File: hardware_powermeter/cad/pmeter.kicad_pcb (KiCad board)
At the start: 4 copper layers, 60 x 16 mm, 57 parts, among them J101 conector magnetico 6 vias, J102 JST SM02B-SRSS-TB, J201 Tag-Connect TC2030-NL, J301 furos da ponte, U101 nPM1100-QDAB, U102 MAX17048G+T10, U201 MinewSemi ME54BS13, U301 ADS1220IRVAR, U302 TPS22916BYFPR, U401 BMA400, U402 TMP117AIDRVR

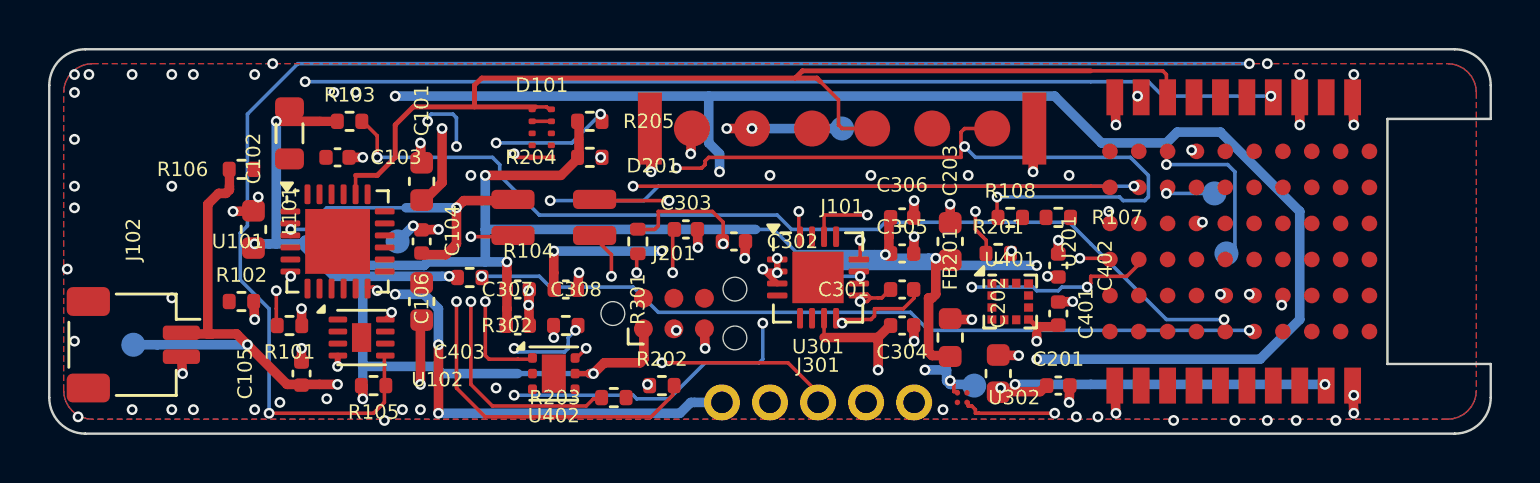
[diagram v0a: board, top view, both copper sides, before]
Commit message: feat(hardware): 48 x 16 mm board and a 53,4 x 19,4 x 8,5 mm pod
The board came down from 60 to 48 mm and the pod from 65,4 x 19,4 x 10,5
to 53,4 x 19,4 x 8,5, with the mass estimate at 11,4 g against the 20 g
of the class. The height now meets the target exactly, because the cell
shrank from 4,0 to 2,5 mm: the owner's 5 kOhm decision takes the meter
from 3,9 to 1,5 mA while pedalling, so 50 hours ask for about 75 mAh and
a 100 mAh pouch is enough. The six-way connector stays, in two rows of
three instead of a single row, which gave back about 7 mm of length
without losing a way, and the Tag-Connect went: with SWD on the cable it
was duplicated copper.

It is NOT manufacturable yet, and the numbers say why rather than a
hopeful adjective: the design rule check finds 0 errors but 16
connections still open. One of them, ERR_N, has no copper at all while
the router reported "98 routed, 0 nets left out", so the router's own
accounting is wrong, not just its routing. Disabling the pruning of
dangling tracks was tried first and changed nothing, which clears the
pruning. A second routing pass made it worse, 21 open and three pairs of
vias too close: the pass is not incremental, it re-routes from scratch
into a different result.

Two more real defects are recorded: the placer cannot seat C403 and
C308, carrying them 11 to 13 mm from the part they decouple, and three
pod rules fail, the back-face bodies against the cell, the rib at zero
and a back pad under a pillar.

The layer drawings print properly for the first time. kicad-cli 8.0.6
does not have --page-size-mode or --exclude-drawing-sheet, which are
KiCad 9 options, so the export was failing outright and, before that,
putting a 1:1 board in the corner of an empty sheet. The flags are now
tried and dropped if unknown, and the board is cropped with fitz
instead: 5:1, centred, scale bar and title block.
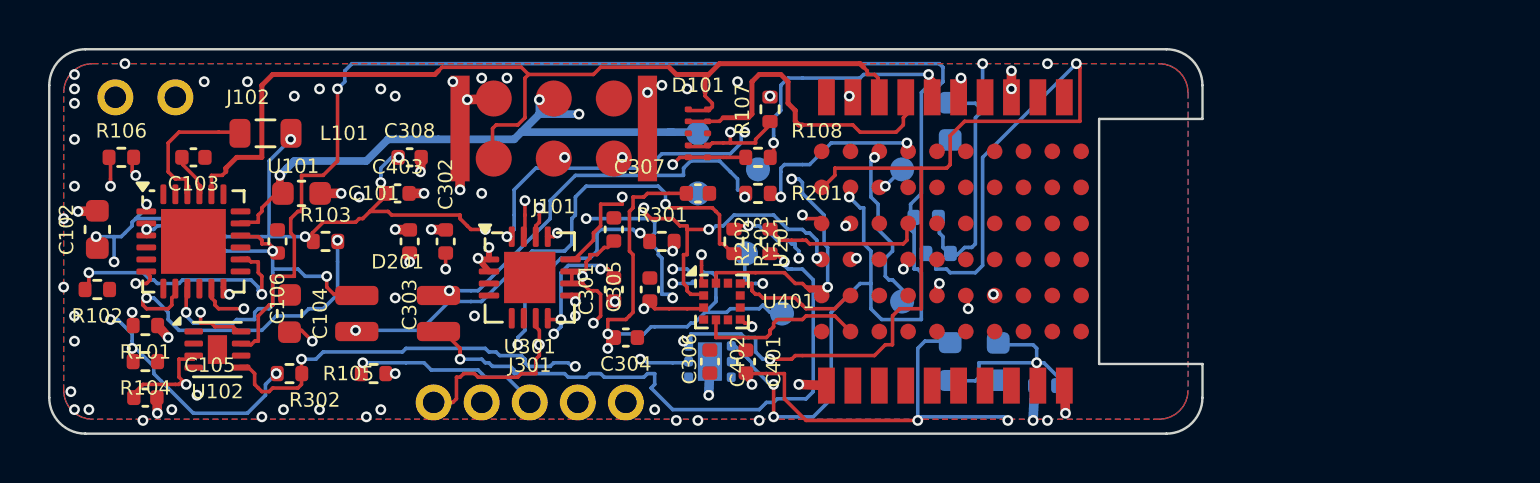
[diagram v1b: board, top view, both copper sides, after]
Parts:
- removed J201: Tag-Connect TC2030-NL, Connector:Tag-Connect_TC2030-IDC-NL_2x03_P1.27mm_Vertical
- C201, C202, C203, FB201, R204, R205, U302, U402: moved to B.Cu
- J101: footprint pmeter:Pogo_Magnetico_6P_P2.5mm -> pmeter:Pogo_Magnetico_6P_2x3_P2.5mm
- J102: value JST SM02B-SRSS-TB -> furos da celula; footprint Connector_JST:JST_SH_SM02B-SRSS-TB_1x02-1MP_P1.00mm_Horizontal -> pmeter:Furos_Celula_2x1.5mm_P2.5mm
- moved TP102 24.3 mm to (52.0, 31.0)
- moved TP103 17.0 mm to (54.0, 33.5)
- moved TP104 15.3 mm to (54.5, 30.0)
- moved C402 15.0 mm to (52.5, 38.0)
- moved R204 15.0 mm to (62.0, 33.5)
- moved R205 14.6 mm to (61.5, 32.0)
- moved R104 13.9 mm to (29.0, 38.0)
- moved TP201 13.6 mm to (60.5, 35.5)
- moved C401 13.2 mm to (54.0, 38.0)
- moved TP202 13.0 mm to (60.5, 30.0)
- moved R107 12.8 mm to (55.0, 27.5), turned to 90 degrees
- moved U302 12.1 mm to (52.0, 34.5)
- moved C305 12.0 mm to (48.5, 32.5), turned to 90 degrees
- moved C301 12.0 mm to (48.5, 35.0), turned to 90 degrees
- moved C302 12.0 mm to (41.5, 33.0), turned to 90 degrees
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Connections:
- U201 pad 4: RESET -> (no net)
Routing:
- net 3V0_EXC: track 114.0 -> 31.1 mm, vias 11 -> 3
- net RESET: track 73.4 -> 0.00 mm, vias 3 -> 0
- net LED_G: track 62.6 -> 6.76 mm, vias 4 -> 0
- net I2C_SDA: track 38.6 -> 76.6 mm, vias 4 -> 6
- net GAUGE_ALRT: track 72.3 -> 36.4 mm
- net SWCLK_J: track 40.0 -> 5.65 mm, vias 4 -> 2
- net ERR_N: track 33.0 -> 0.00 mm, vias 2 -> 0
- net I2C_SCL: track 43.1 -> 72.4 mm, vias 5 -> 4
- net CHG_N: track 40.8 -> 14.1 mm
- net SPI_SCK: track 0.00 -> 24.6 mm, vias 0 -> 3
- net LED_KG: track 7.50 -> 25.4 mm
- net 3V0: track 107.1 -> 124.6 mm, vias 13 -> 22
- net LED_KR: track 32.9 -> 16.8 mm
- net SPI_MISO: track 0.00 -> 16.1 mm, vias 0 -> 3
- net GND: track 30.0 -> 16.5 mm, vias 81 -> 63
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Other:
- board size 60 x 16 mm -> 48 x 16 mm
- board text added: "56 pecas colocadas; a ponte de extensometros vive no braco e chega pelos pads J301"
- board text added: "BIKE POWER METER - placa 48 x 16 mm, 0.8 mm, 4 camadas"
- board text removed: "57 pecas colocadas; a ponte de extensometros vive no braco e chega pelos pads J301"
- board text removed: "BIKE POWER METER - placa 60 x 16 mm, 0.8 mm, 4 camadas"

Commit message: fix(hardware): let the DRC judge the routing, and fit the pod to the board
No stage of the router could tell whether it had connected anything. The
negotiated-congestion stage closed announcing "96 connections, 0 contested
cells" while eleven pads had no copper at all, among them every terminal of
USB_DM, which was left as three loose fragments of 0.9 mm. Three separate
defects, each measured:

  - the acceptance test compared the NUMBER of connections (n_ok_n > n_ok)
    instead of open pads;
  - accepting the negotiated answer threw away the sequential copper of the
    nets it had not routed (16 -> 12 open once inherited);
  - the inherited copper was not given to the negotiated stage as an
    obstacle, so it planned over an empty board (182 violations, down to 25
    with pre_seg/pre_via).

So the judge is now KiCad. reparar.py reads _drc_all.json, rebuilds the grid
from the copper that is really on the board and routes what the DRC still
calls open, with the same clearances and pad necks. It always starts at a
PAD: starting at a track end makes the search find a target on that very
track and emit a stub joining it to itself, which is how five connections
were reported closed without closing.

A via is not free either. It pierces every layer, so it has to clear every
net on all of them; placed blind to touch a pad it landed on C201's
3V0_MOD pad and cost two shorts, a hole clearance and a mask bridge - for a
connection that did not even close. route.via_cabe_aqui checks first.

SO_FRENTE becomes a preference. The USB pair was calculated as 90 ohm
microstrip on F.Cu, but as a law it leaves USB_DM unroutable: 16.7 mm to
U101 and 8.3 to U201 across a full top face. This is full speed, 12 Mbit/s,
where make_pro.py already recorded that extra clearance bought nothing.
The search tries the front at both slacks and only changes layer when there
is no way, saying so when it does.

On the board and the pod:

  - C307, C308 and C403 decouple chips that live on the BACK a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
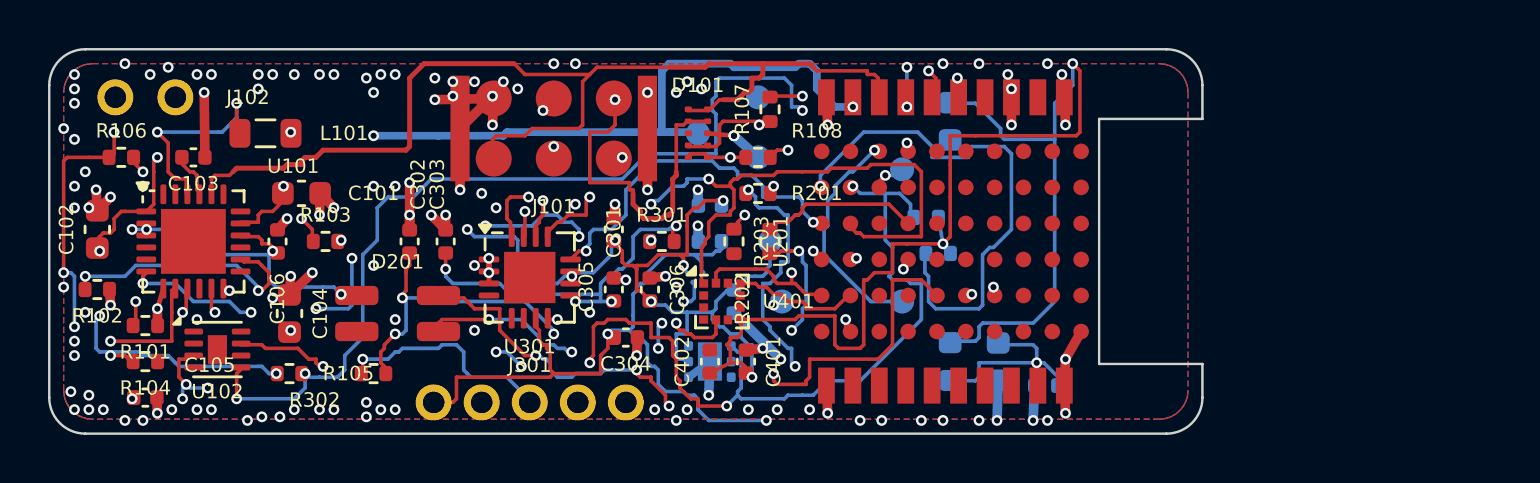
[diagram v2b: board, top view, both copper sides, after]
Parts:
- C307, C308, C403: moved to B.Cu
- moved C403 14.7 mm to (53.5, 35.5), turned to 90 degrees
- moved C308 12.7 mm to (52.5, 31.5)
- moved TP102 4.72 mm to (54.5, 27.0)
- moved C307 2.06 mm to (52.5, 33.0)
- moved TP103 1.12 mm to (55.0, 33.0)
- moved TP104 0.50 mm to (54.5, 29.5)
- moved TP301 0.50 mm to (55.5, 35.5)
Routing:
- net I2C_SDA: track 76.6 -> 21.7 mm, vias 6 -> 1
- net GND: track 16.5 -> 50.9 mm, vias 63 -> 132
- net I2C_SCL: track 72.4 -> 49.4 mm, vias 4 -> 6
- net LED_KB: track 21.4 -> 0.00 mm, vias 2 -> 0
- net GAUGE_ALRT: track 36.4 -> 52.8 mm, vias 3 -> 4
- net USB_DM: track 13.8 -> 29.1 mm, vias 0 -> 3
- net SPI_MISO: track 16.1 -> 29.6 mm
- net LED_KR: track 16.8 -> 30.0 mm, vias 2 -> 5
- net SHPACT: track 55.1 -> 46.3 mm, vias 2 -> 7
- net ADC_CS: track 22.7 -> 30.8 mm, vias 3 -> 2
- net 3V0_EXC: track 31.1 -> 37.5 mm
- net VBUS: track 37.2 -> 42.2 mm
- net CHG_N: track 14.1 -> 18.9 mm, vias 2 -> 4
- net IMU_INT1: track 7.10 -> 11.5 mm, vias 0 -> 2
- net USB_DP: track 41.1 -> 45.0 mm
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
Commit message: feat(hardware): draw the module for real, and bond the pod to flat metal
Two things the owner asked for, and one the second of them found.

The module gets a body instead of a box. Every DIMENSION is off the maker's
mechanical drawing - the one the footprint is generated from, which closes on
itself three independent ways - and every COLOUR is read off the product
photo, and that difference is recorded rather than smoothed over: a dimension
that closes three ways is evidence, a colour from a photograph is a reading.
It is not one box, because the part is not one box and drawing it as one
hides what decides the layout: a BLACK printed circuit (Holyiot's photo, not
the green of the ME54BS13), a shield can that reads dark rather than as
bright tin, the CERAMIC ANTENNA as an ivory block with metallised ends
sitting outside the can in the 3,80 mm band the drawing keeps clear of pads,
and the gold pads on the underside. Forty-one solids.

It is drawn 2,40 mm tall, and that is a RESERVATION, not a measurement: the
advert gives no height at all. A can over a 0,80 mm board runs 1,8 to 2,2 in
this class, so 2,40 has margin, and drawing it at the reservation makes the
body, the lid's ceiling and the new rule PD18 carry the same number - a part
that arrives taller is then caught by a rule instead of by a lid that will
not close.

The owner asked for the open questions to be measured rather than waited for,
so each one became a requirement with a rule that checks it. The crank's
numbers are the CLASS's - Shimano 105 and Ultegra, the narrow end of the
arm's taper, the tight end of road frame clearance - and PD17 measures the
pod against them. It failed on the first run, and the finding is real: the
arm's inner face is not flat across. A fillet of about 2,5 mm on each side
leaves only 15 of the class's 20 mm flat, and a 19,0 mm pod bonded across its
whole underside would sit on those radii on both sides - adhesive thick at
the edges, thin in the middle, and a joint that peels from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
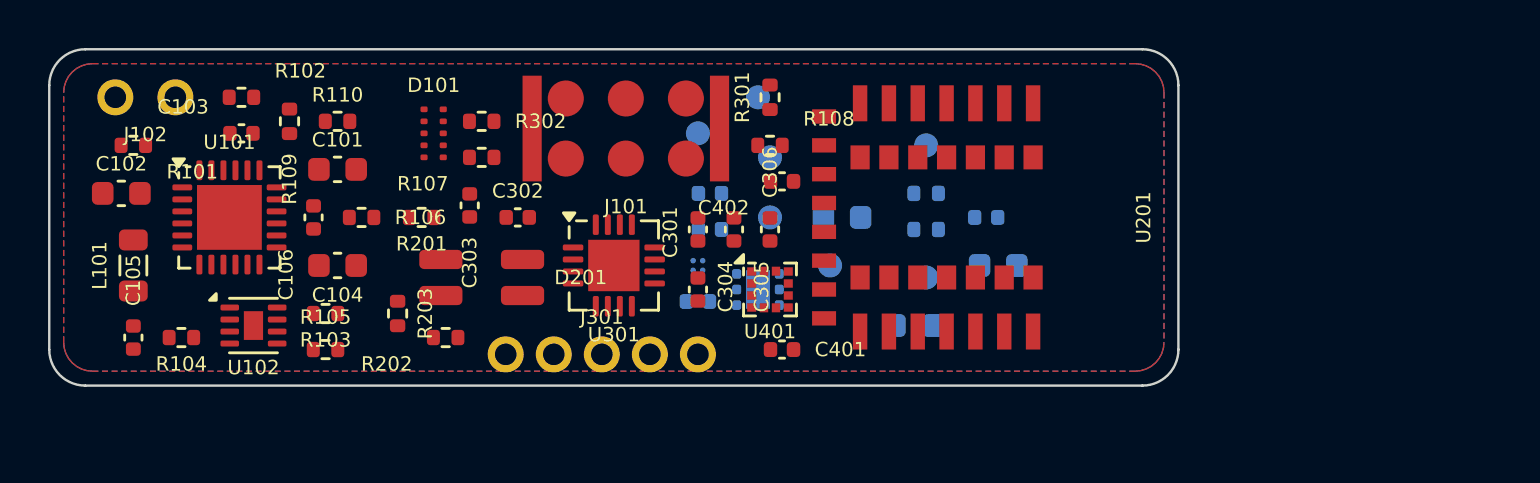
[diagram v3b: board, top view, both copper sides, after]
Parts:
- added R109: 1 M, Resistor_SMD:R_0402_1005Metric, F.Cu at (35.0, 28.0)
- added R110: 470 k, Resistor_SMD:R_0402_1005Metric, F.Cu at (37.0, 28.0)
- U201: value MinewSemi ME54BS13 -> HOLYIOT-26001-A; footprint pmeter:MinewSemi_ME54BS13_16.5x12mm -> pmeter:HOLYIOT_26001A_10x12.5mm
- moved R203 14.3 mm to (39.5, 36.0)
- moved R202 14.1 mm to (41.5, 37.0), turned to 0 degrees
- moved R201 14.0 mm to (40.5, 32.0)
- moved R107 12.2 mm to (43.0, 29.5), turned to 0 degrees
- moved R302 11.4 mm to (43.0, 28.0)
- moved D101 11.0 mm to (41.0, 28.5)
- moved R106 10.3 mm to (38.0, 32.0)
- moved R102 10.0 mm to (33.0, 27.0)
- moved C402 8.08 mm to (55.5, 30.5), turned to 0 degrees
- moved L101 7.78 mm to (28.5, 34.0), turned to 90 degrees
- moved R101 7.52 mm to (28.5, 29.0)
- moved R301 7.50 mm to (55.0, 27.0), turned to 90 degrees
- moved C201 7.43 mm to (64.0, 32.0)
- moved C203 6.02 mm to (58.0, 32.0), turned to 0 degrees
- moved C306 5.59 mm to (55.0, 32.5)
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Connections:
- D101 pad 1: USB_DP -> UART_TX
- D101 pad 10: USB_DP -> UART_TX
- D101 pad 2: USB_DM -> UART_RX
- D101 pad 9: USB_DM -> UART_RX
- J101 pad 3: USB_DM -> UART_RX
- J101 pad 4: USB_DP -> UART_TX
- U101 pad 19: USB_DM -> UART_RX
- U101 pad 20: USB_DP -> UART_TX
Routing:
- net 3V0: track 127.0 -> 0.00 mm, vias 16 -> 0
- net GAUGE_ALRT: track 52.8 -> 0.00 mm, vias 4 -> 0
- net GND: track 50.9 -> 0.00 mm, vias 132 -> 0
- net I2C_SCL: track 49.4 -> 0.00 mm, vias 6 -> 0
- net SHPACT: track 46.3 -> 0.00 mm, vias 7 -> 0
- net USB_DP: track 45.0 -> 0.00 mm
- net VBUS: track 42.2 -> 0.00 mm, vias 4 -> 0
- net 3V0_EXC: track 37.5 -> 0.00 mm, vias 3 -> 0
- net ADC_CS: track 30.8 -> 0.00 mm, vias 2 -> 0
- net LED_KR: track 30.0 -> 0.00 mm, vias 5 -> 0
- net SPI_MISO: track 29.6 -> 0.00 mm, vias 3 -> 0
- net USB_DM: track 29.1 -> 0.00 mm, vias 3 -> 0
- net VBAT: track 26.5 -> 0.00 mm, vias 8 -> 0
- net LED_KG: track 22.0 -> 0.00 mm, vias 4 -> 0
- net I2C_SDA: track 21.7 -> 0.00 mm, vias 1 -> 0
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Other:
- board size 48 x 16 mm -> 47 x 14 mm
- board text added: "58 pecas colocadas; a ponte de extensometros vive no braco e chega pelos pads J301"
- board text added: "BIKE POWER METER - placa 47 x 14 mm, 0.8 mm, 4 camadas"
- board text removed: "56 pecas colocadas; a ponte de extensometros vive no braco e chega pelos pads J301"
- board text removed: "BIKE POWER METER - placa 48 x 16 mm, 0.8 mm, 4 camadas"

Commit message: feat(all): 114 h instead of 52, a real cell, and a pod that finally shrank
Three things the owner pushed back on, and one arithmetic error of this
project's own that the pushing uncovered.

THE POD HAD NOT SHRUNK, and he was right. The board went from 51 x 16 to
47 x 14 with the smaller module, and the pod went from 56,4 to 59,4 - the
two closing screws had each been given a boss OUTSIDE the board, at 5,4 mm
of length. The right-hand screw now goes THROUGH the board: a boss rises
from the floor, a 2,00 mm neck passes through a hole, and the screw comes
down from the lid. It can only be done on one side - a post that pierces
the board needs floor under it with no cell, and the cell leaves an 8,5 mm
window between its end and the module - so the left screw keeps its boss in
the cell's own wire channel. 55,7 x 19,0 now.

THE CELL WAS AN ARITHMETIC ERROR. docs/02 carried "a 100 mAh cell is 2,5 mm
thick", and no cell of 23 x 11 mm is 100 mAh at any thickness: calibrating
small LiPo pouches on four standard sizes gives 0,077 mAh/mm3, so 2,5 mm
held ~49 mAh and 32 h against a requirement of 50. The 8,5 mm pod only ever
closed because the capacity was wrong. The owner chose 4,0 mm of cell and a
10,0 mm pod - still inside the class reference, which runs to 13.

The cell's LENGTH is 23 and not 25, and that too is measured: at 24 and 25
its shadow reaches past x 28 on the back face and the ferrite and the
rail-side reservoir lose their place. 23 x 11 x 4,0 is ~78 mAh.

AND THEN THE ARITHMETIC THAT WAS NEVER DONE. docs/02 had both numbers of the
ADS1220's duty-cycle mode - the converter falls from 0,585 to 0,190 mA, and
the bridge runs 30 % of the time because the PSW that feeds it opens with it
(SBAS501D 8.3.9) - but it never multiplied the two with the 5 kOhm bridge:
its table only tried duty-cycle against 1 kOhm, from when the bridge WAS
1 kOhm. Together they cut 55 % of the current:

    5 kOhm continuous    0,600 + 0,585 + 0,300 = 1,50 mA ->  52 h
    5 kOhm duty-cycle    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
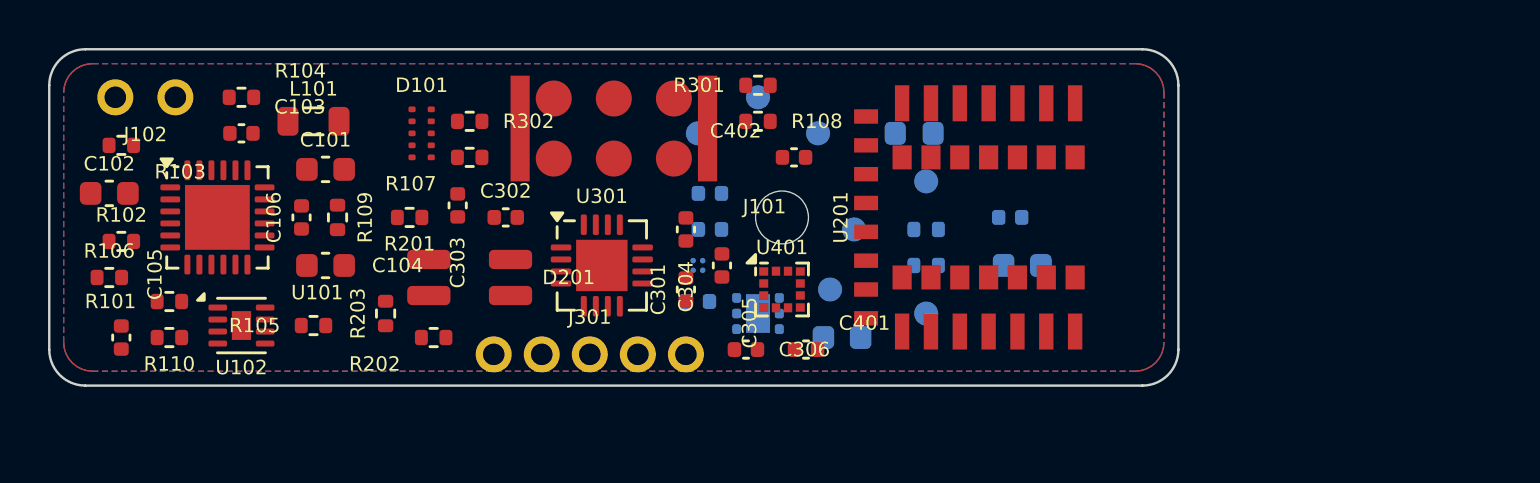
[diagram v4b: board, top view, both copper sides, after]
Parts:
- added REF**: MountingHole_2.2mm_M2, MountingHole:MountingHole_2.2mm_M2, F.Cu at (55.5, 32.0)
- moved R110 11.4 mm to (30.0, 37.0)
- moved R103 11.0 mm to (28.0, 29.0)
- moved R106 10.8 mm to (27.5, 34.5)
- moved R104 10.3 mm to (33.0, 27.0)
- moved L101 9.60 mm to (36.0, 28.0), turned to 0 degrees
- moved FB201 8.00 mm to (61.0, 28.5)
- moved R102 7.81 mm to (28.0, 33.0)
- moved TP202 7.00 mm to (61.5, 36.0)
- moved R101 6.67 mm to (30.0, 35.5)
- moved TP104 6.04 mm to (57.5, 35.0)
- moved C306 5.10 mm to (54.0, 37.5), turned to 0 degrees
- moved C203 5.00 mm to (58.0, 37.0)
- moved R109 4.47 mm to (37.0, 32.0)
- moved TP103 4.03 mm to (57.0, 28.5)
- moved TP201 4.00 mm to (61.5, 30.5)
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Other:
- board text added: "1 furos; empilhamento assimetrico 0.1 / 0.46 / 0.1 mm, o mesmo do ciclocomputador"
- board text removed: "0 furos; empilhamento assimetrico 0.1 / 0.46 / 0.1 mm, o mesmo do ciclocomputador"
